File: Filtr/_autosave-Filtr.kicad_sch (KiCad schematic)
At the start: 38 parts, among them J1 Jack-DC, J2 Conn_01x04_Pin, SW3 RotaryEncoder_Switch, U1 TPS562200, U2 STM32G030K6Tx

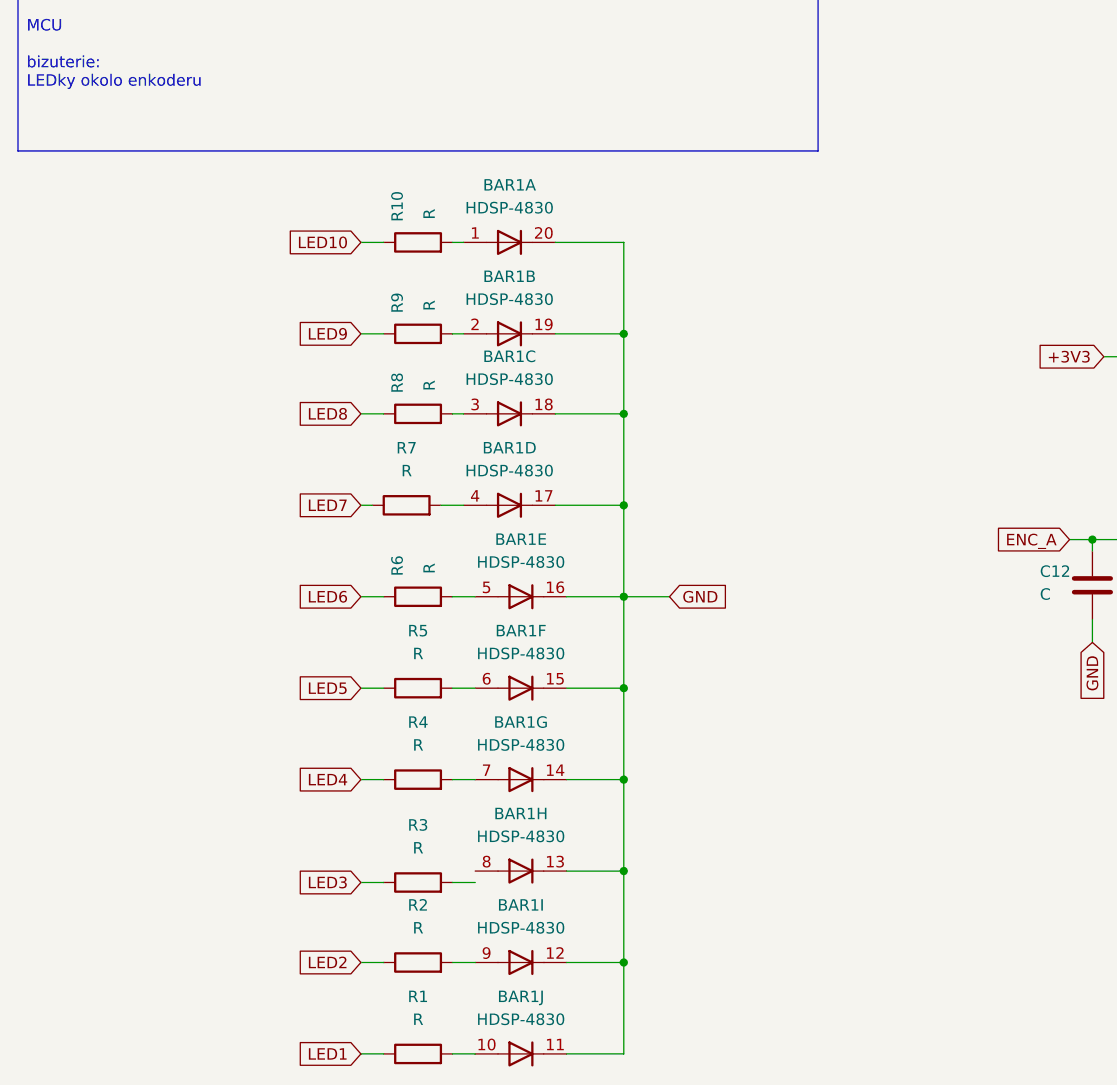
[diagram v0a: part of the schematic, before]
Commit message: Kicad - pridani bargarfu a shiftregistru
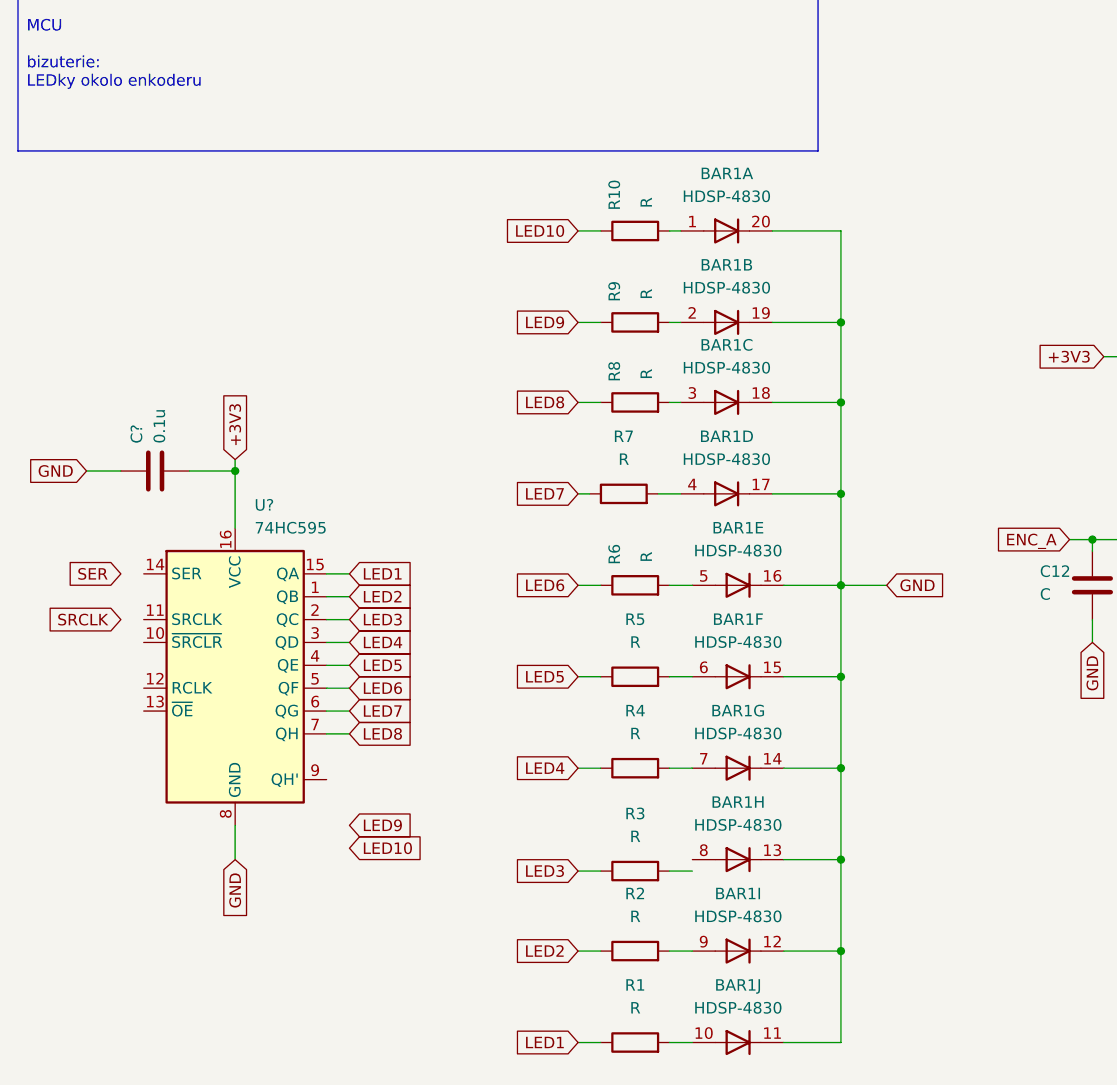
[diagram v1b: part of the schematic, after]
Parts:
- added C?: 0.1u, Capacitor_SMD:C_0603_1608Metric, symbol Device:C
- added U?: 74HC595, symbol 74xx:74HC595
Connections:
- net +3V3: now also C?.1, U?.16 (VCC)
- net GND: now also C?.2, U?.8 (GND)
- net LED1: now also U?.15 (QA)
- net LED2: now also U?.1 (QB)
- net LED3: now also U?.2 (QC)
- net LED4: now also U?.3 (QD)
- net LED5: now also U?.4 (QE)
- net LED6: now also U?.5 (QF)
- net LED7: now also U?.6 (QG)
- net LED8: now also U?.7 (QH)
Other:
- moved on the sheet: BAR1A, BAR1B, BAR1C, BAR1D, BAR1E, BAR1F, BAR1G, BAR1H, BAR1I, BAR1J, R1, R10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
